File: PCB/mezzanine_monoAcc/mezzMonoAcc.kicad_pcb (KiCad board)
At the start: 2 copper layers, 13 parts, among them J1 Conn_02x20_Odd_Even, J10 Conn_02x03_Odd_Even, J11 Conn_01x02, J12 Conn_01x02, J13 Conn_01x02, J2 Conn_01x02, J3 Conn_01x02, J4 Conn_01x02, J5 Conn_01x02, J6 Conn_01x02, J7 Conn_02x03_Odd_Even, J8 Conn_01x02, J9 Conn_02x07_Odd_Even

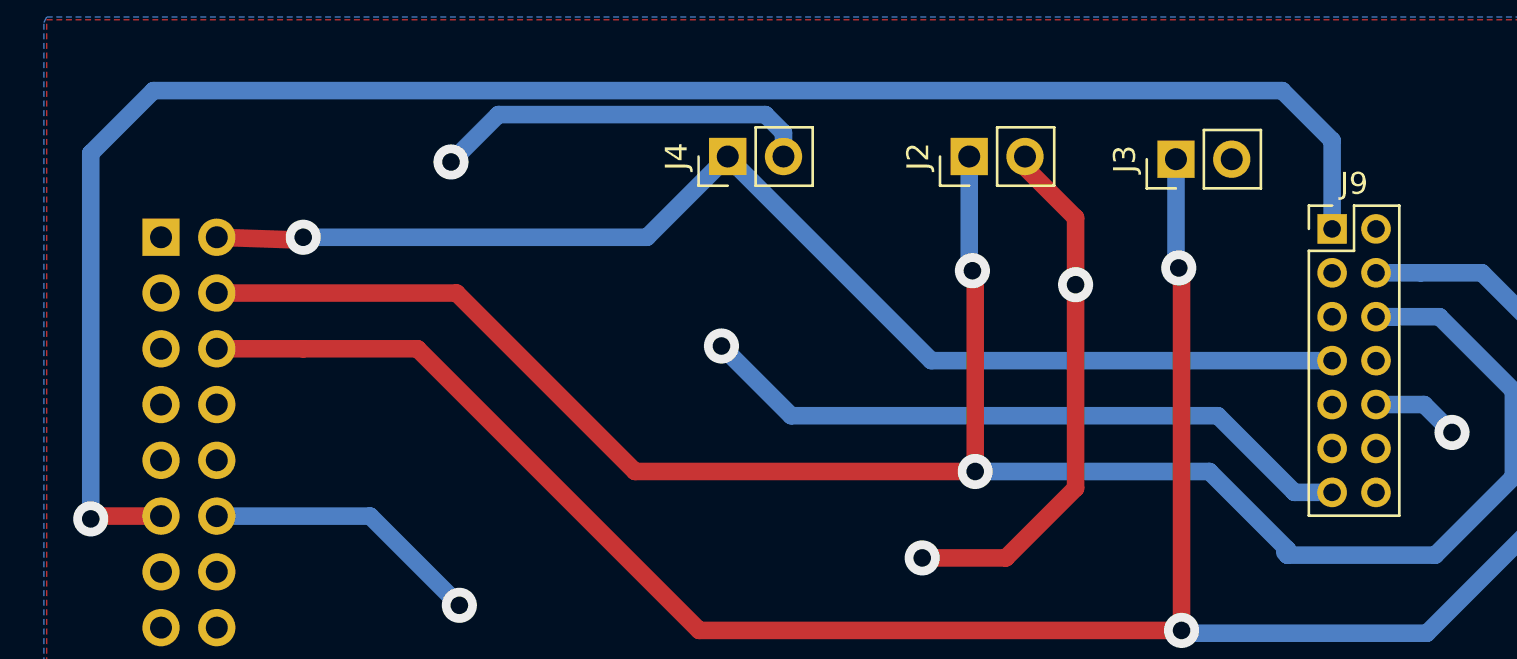
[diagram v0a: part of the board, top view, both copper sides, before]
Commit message: fix error pin assignment - 5v DAC pin2
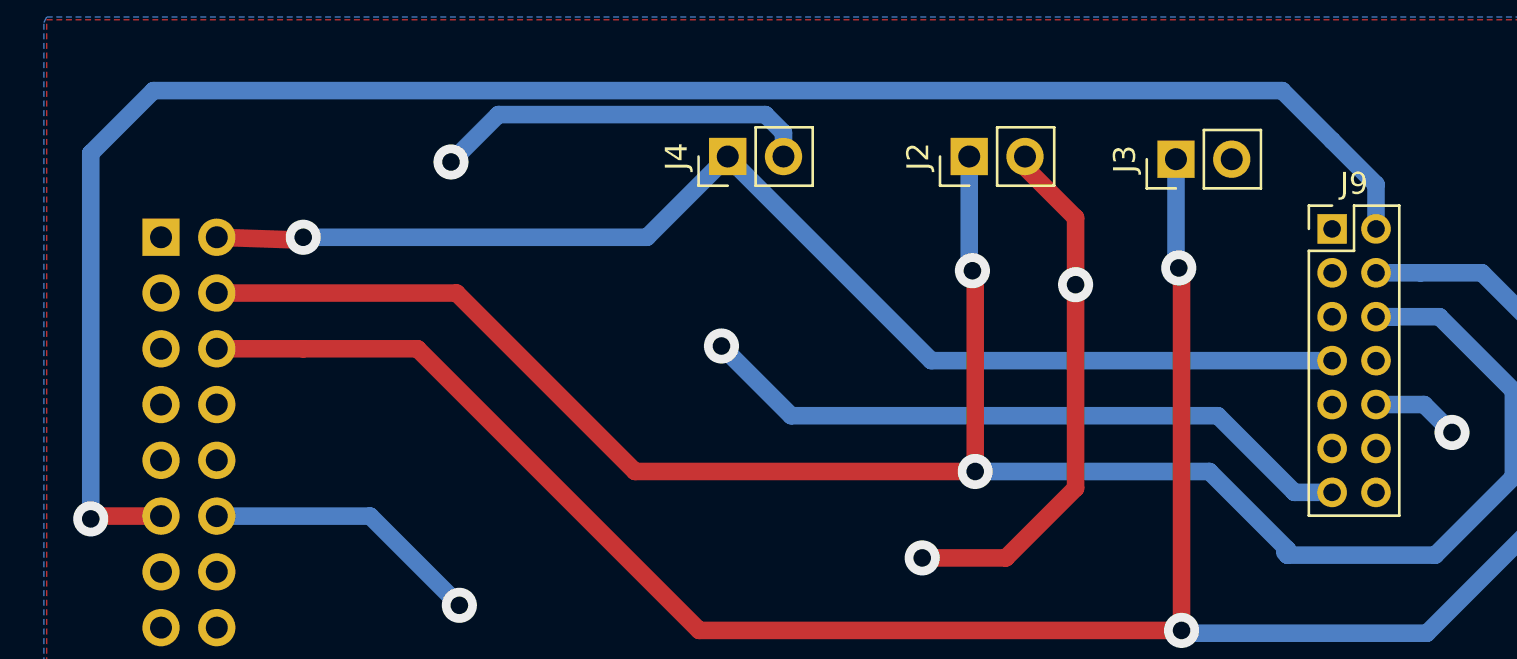
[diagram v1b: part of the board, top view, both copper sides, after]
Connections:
- J9 pad 1: /VDD(5V) -> Net-(J9-Pad1)
- J9 pad 2: Net-(J9-Pad2) -> /VDD(5V)
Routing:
- net /VDD(5V): track 82.8 -> 83.6 mm
